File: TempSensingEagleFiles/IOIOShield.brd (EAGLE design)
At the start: 33 x 58.4 mm, 3 parts

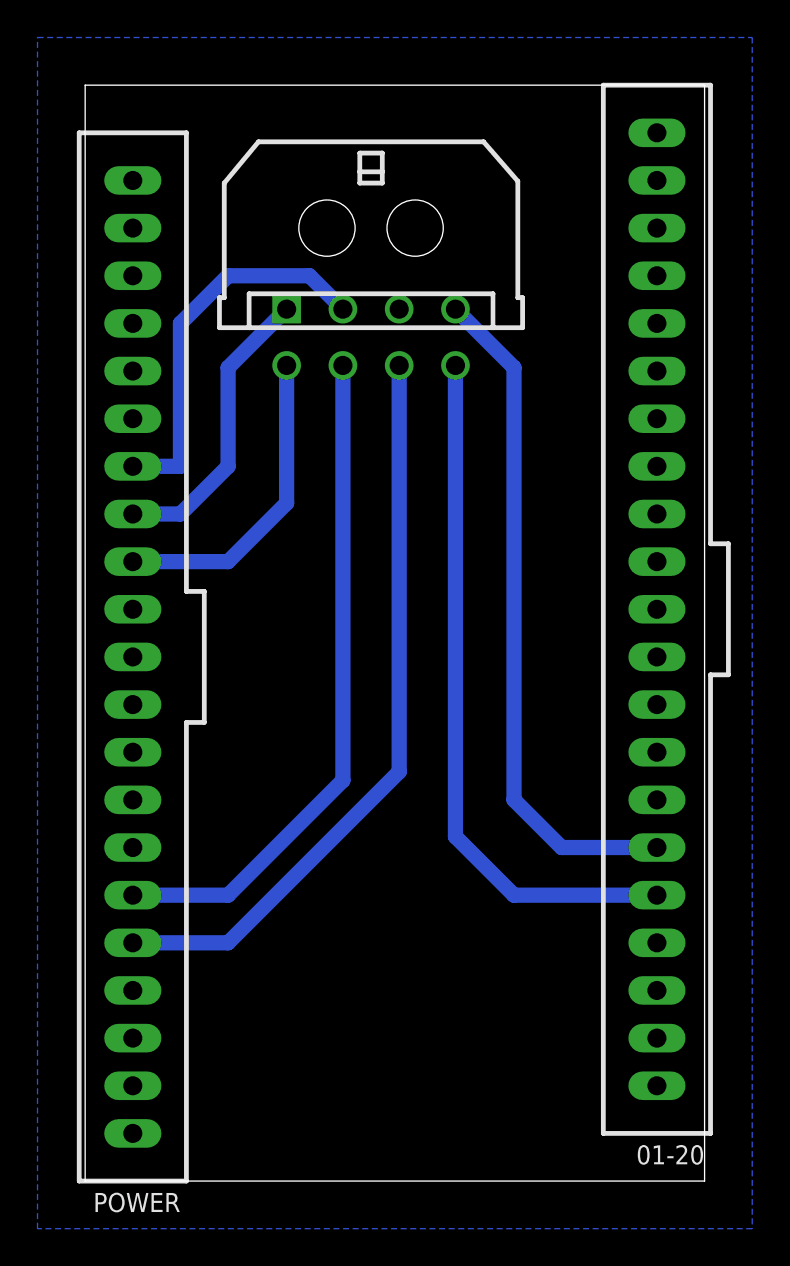
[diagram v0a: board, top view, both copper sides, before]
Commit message: STABLE: working with only one sensor
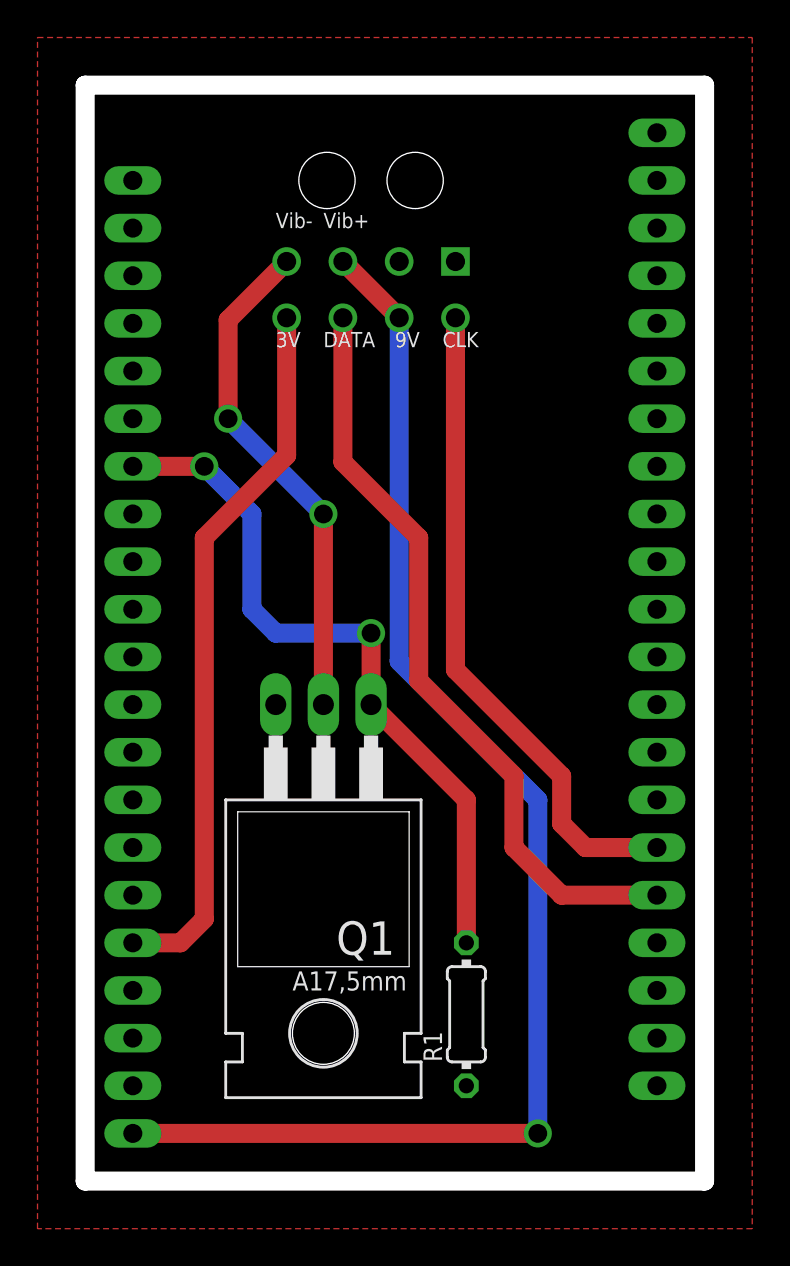
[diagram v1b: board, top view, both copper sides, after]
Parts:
- removed X4: (no value), con-molex-micro-fit-3_0:43045-0800
- added Q1: IRF3704, transistor-power:TO220AH
- added R1: 10K, rcl:0204/7
- added X1: (no value), con-molex-micro-fit-3_0:43045-0800
- flipped 01-20 to the bottom
- flipped POWER to the bottom
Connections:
- removed net N$4: POWER.6, X4.P$6
- new net GND: 01-20.1, POWER.2, Q1.E, R1.1, X1.P$1, X1.P$2
- net N$1: now also Q1.B, R1.2; no longer X4.P$2
- net N$2: now also Q1.C, X1.P$4; no longer POWER.14, X4.P$1
- net N$3: now also POWER.1, X1.P$3, X1.P$6; no longer POWER.13, X4.P$5
- net N$5: now also X1.P$8; no longer X4.P$7
- net N$6: now also X1.P$5; no longer X4.P$4
- net N$8: now also X1.P$7; no longer X4.P$8
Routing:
- net N$3: track 16.8 -> 72.4 mm, vias 0 -> 1
- net N$4: track 35.9 -> 0.00 mm
- net N$1: track 20.6 -> 38.0 mm, vias 0 -> 2
- net N$2: track 16.0 -> 27.0 mm, vias 0 -> 2
- net N$8: track 37.2 -> 40.7 mm
- net N$5: track 39.6 -> 38.2 mm
- net N$6: track 36.1 -> 34.9 mm
- added copper zone on layer 1, net GND
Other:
- board text added: "3V"
- board text added: "9V"
- board text added: "CLK"
- board text added: "DATA"
- board text added: "Vib+"
- board text added: "Vib-"
